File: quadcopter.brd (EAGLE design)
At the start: 151.1 x 125.5 mm, 66 parts, among them J1 AVR_SPI_PRG_6NS, Q1 2.6A, Q2 2.6A, Q3 2.6A, Q4 2.6A, U1 ATMEGA128RFA1, U2 IMU_LSM9DS1TR, Y1 16MHz

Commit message: tried some stuff on board
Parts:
- moved U2 117.0 mm to (0.00, 0.00), turned to 0 degrees
- moved C23 99.9 mm to (-3.00, 12.0)
- moved C20 98.9 mm to (-9.00, 2.00)
- moved C22 95.6 mm to (-7.00, 12.0)
- moved R8 89.8 mm to (-5.00, -3.00)
- moved C21 89.6 mm to (1.00, 7.00), turned to 0 degrees
- moved C25 86.0 mm to (3.00, 11.0), turned to 180 degrees
- moved U$3 21.2 mm to (91.8, -5.76)
- moved U1 9.85 mm to (165.0, -20.6)

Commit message: added board stuff
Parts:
- moved U1 190.8 mm to (-24.7, -0.20), turned to 270 degrees
- moved U$2 176.4 mm to (-55.9, 2.10), turned to 180 degrees
- moved C2 171.1 mm to (-65.6, 1.80), turned to 180 degrees
- moved D1 151.0 mm to (-56.6, -2.40), turned to 180 degrees
- moved Q1 148.6 mm to (-49.9, -2.20)
- moved Y1 148.3 mm to (-28.4, 10.4), turned to 180 degrees
- moved JP2 147.2 mm to (-29.8, -29.9)
- moved U$1 140.6 mm to (-31.5, 30.2)
- moved C3 138.8 mm to (-45.3, 2.20), turned to 180 degrees
- moved D9 137.4 mm to (-10.0, 28.0), turned to 180 degrees
- moved D5 137.2 mm to (0.03, -27.6), flipped to the bottom, turned to 0 degrees
- moved C16 135.1 mm to (-33.5, 15.2)
- moved U$4 134.8 mm to (2.40, -58.0)
- moved C19 134.0 mm to (-21.5, 29.2), turned to 180 degrees
- moved D6 133.4 mm to (0.00, -27.6), turned to 180 degrees
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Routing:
- added copper zone on layer 2, net 3V
- added copper zone on layer 1, net GND
- added copper zone on layer 15, net GND
- added copper zone on layer 2, net GND
- added copper zone on layer 2, net VBAT
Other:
- board size 151.1 x 125.5 mm -> 185.1 x 185.1 mm

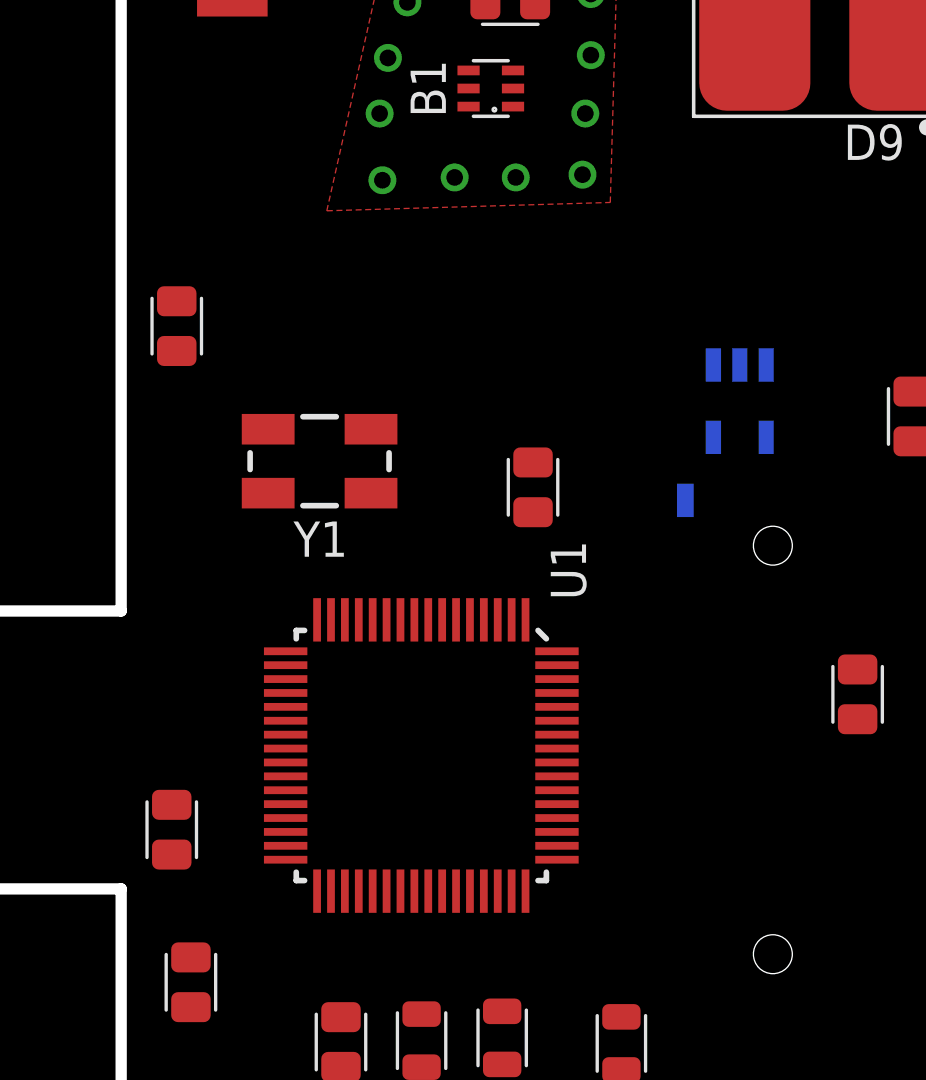
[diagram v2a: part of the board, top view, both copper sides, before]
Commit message: Restricting the Autorouter- setting trace widths - done?
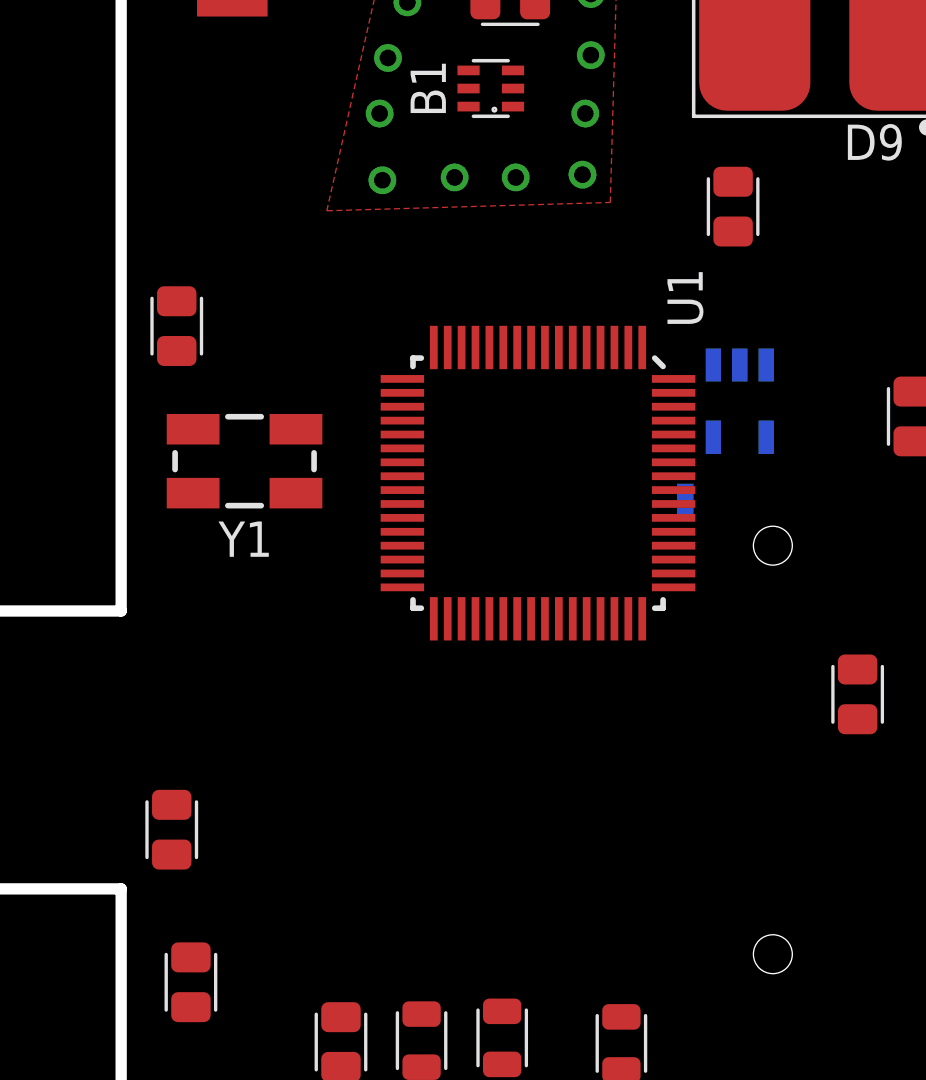
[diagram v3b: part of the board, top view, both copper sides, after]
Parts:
- moved C14 12.4 mm to (-13.5, 19.6)
- moved U1 10.7 mm to (-20.5, 9.60)
- moved Y1 2.70 mm to (-31.1, 10.4)
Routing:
- added copper zone on layer 2, net N$35
- added copper zone on layer 15, net N$36

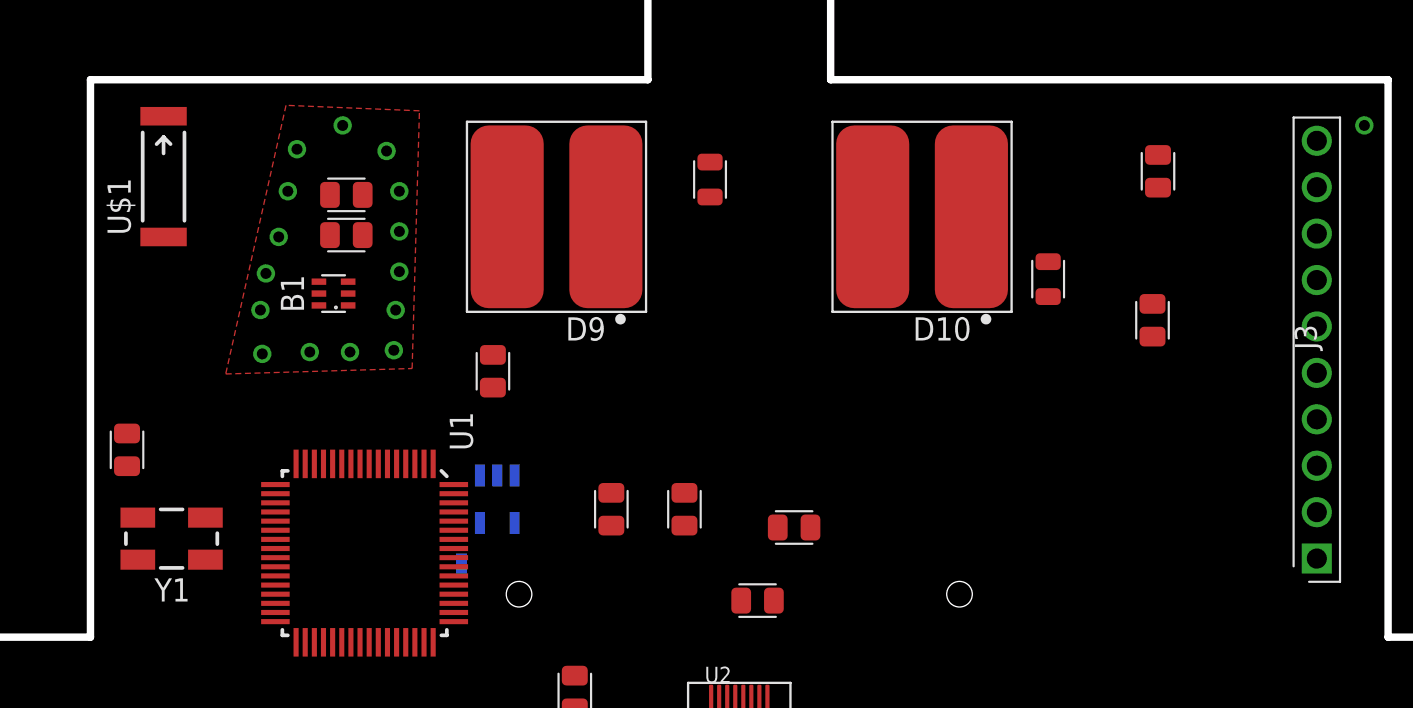
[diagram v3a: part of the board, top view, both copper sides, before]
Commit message: did the imu protection, voltage regulator, breakout header stuff:
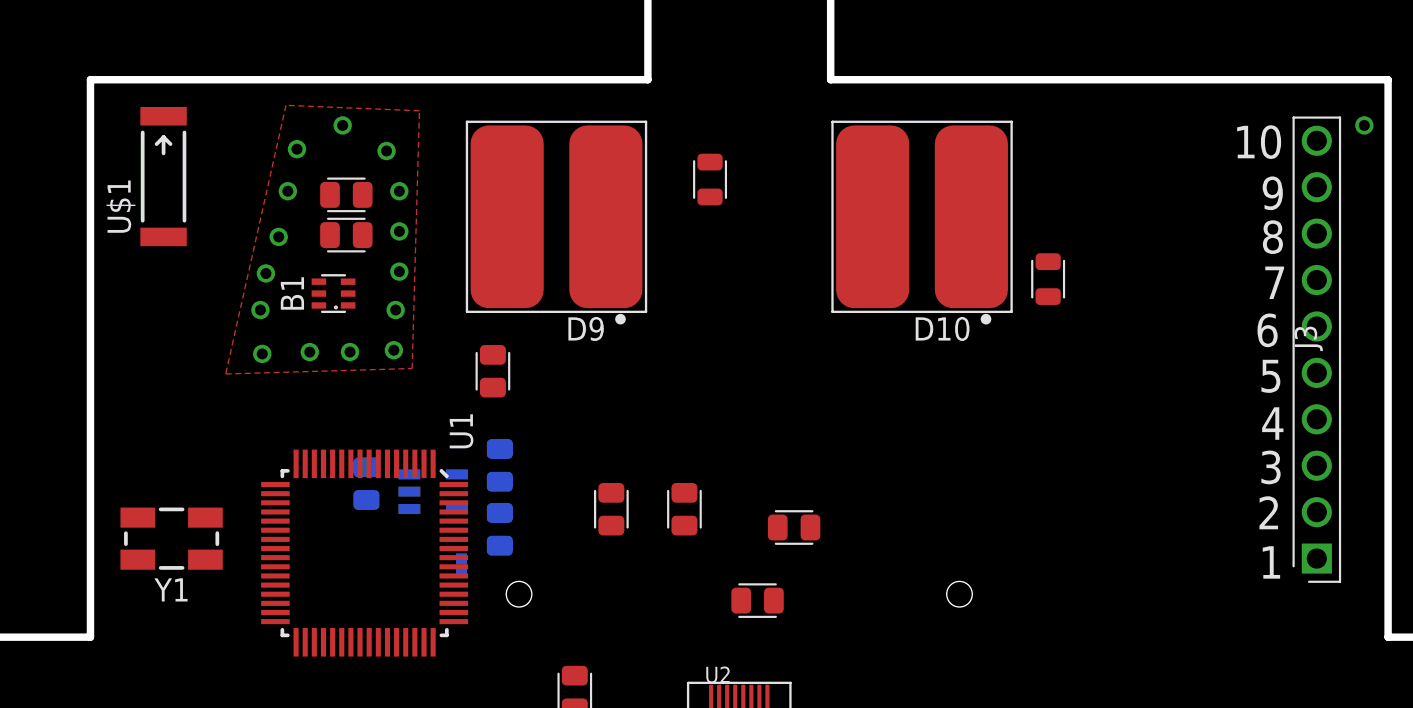
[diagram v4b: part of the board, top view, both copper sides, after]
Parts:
- moved C10 43.9 mm to (-20.4, 13.4), flipped to the bottom, turned to 270 degrees
- moved C11 39.4 mm to (-13.1, 14.4), flipped to the bottom, turned to 270 degrees
- moved C16 20.9 mm to (-13.1, 10.9), flipped to the bottom, turned to 270 degrees
- moved U$3 3.53 mm to (-16.8, 13.0), turned to 90 degrees
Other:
- board text added: "1"
- board text added: "10"
- board text added: "2"
- board text added: "3"
- board text added: "4"
- board text added: "5"
- board text added: "6"
- board text added: "7"
- board text added: "8"
- board text added: "9"

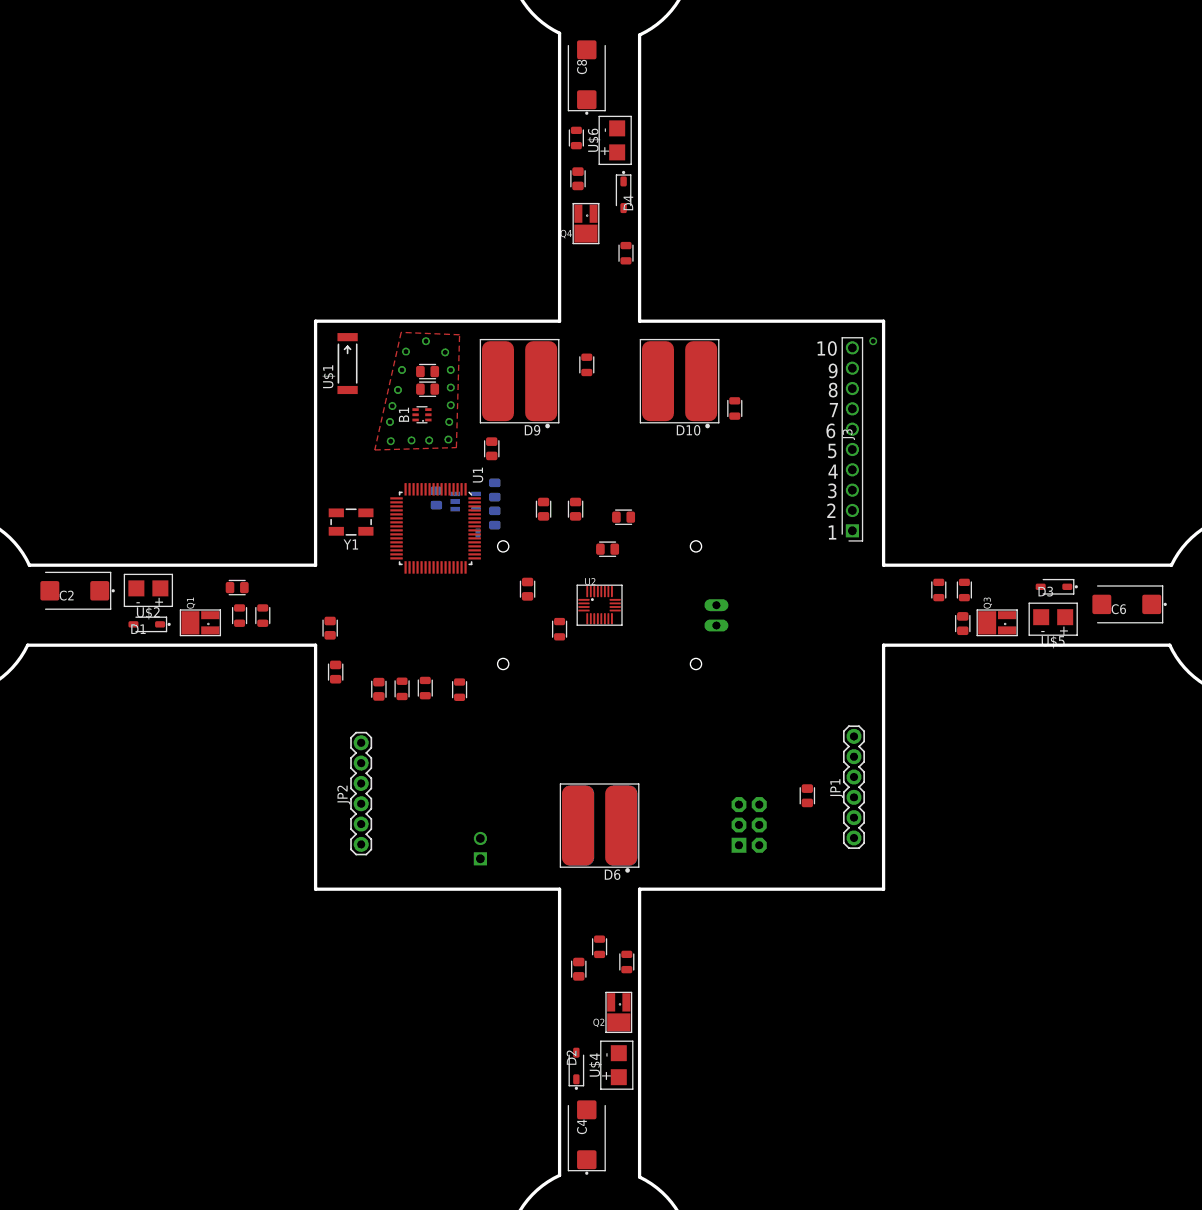
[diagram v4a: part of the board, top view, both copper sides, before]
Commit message: polygons may have fallen apart
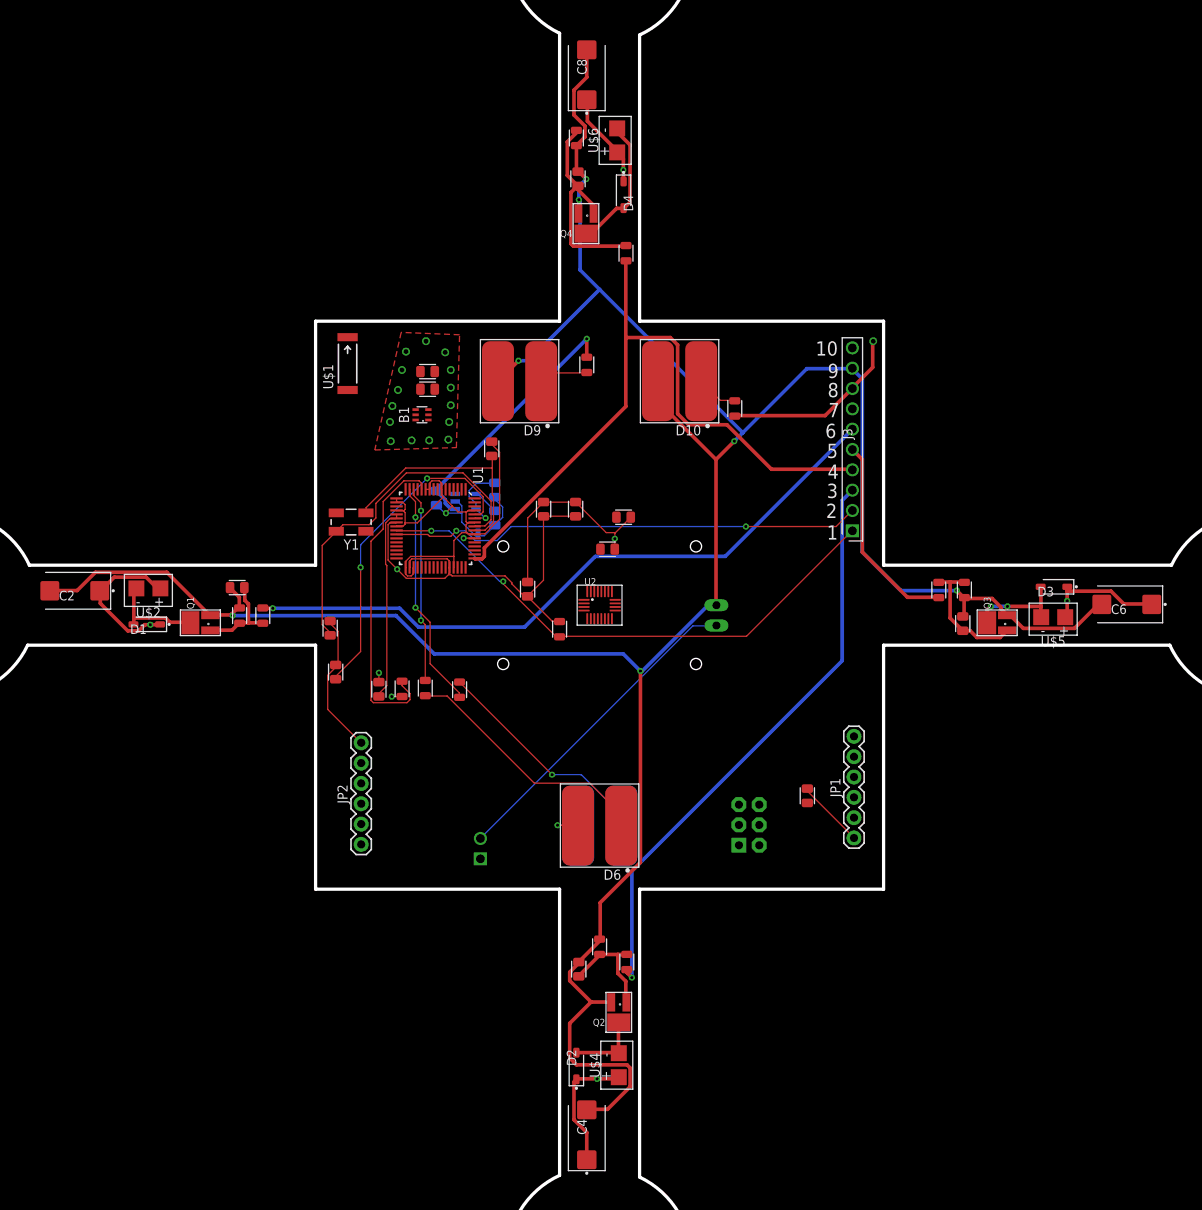
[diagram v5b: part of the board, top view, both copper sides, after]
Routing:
- net BAT_GND: track 0.00 -> 363.1 mm, vias 0 -> 7
- net GND: track 0.00 -> 158.6 mm, vias 15 -> 19
- net VBAT: track 0.00 -> 120.4 mm, vias 1 -> 6
- net PE3: track 0.00 -> 85.9 mm
- net PB5: track 0.00 -> 84.9 mm, vias 0 -> 1
- net PE4: track 0.00 -> 73.6 mm, vias 0 -> 1
- net SCL: track 0.00 -> 68.2 mm, vias 0 -> 2
- net 3V: track 0.00 -> 65.4 mm, vias 0 -> 4
- net SDA: track 0.00 -> 59.4 mm, vias 0 -> 2
- net N$5: track 0.00 -> 43.8 mm
- net N$10: track 0.00 -> 40.9 mm, vias 0 -> 2
- net N$23: track 0.00 -> 40.5 mm
- net RESET: track 0.00 -> 40.1 mm
- net N$28: track 0.00 -> 32.0 mm
- net N$14: track 0.00 -> 29.6 mm
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
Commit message: no more airwires!
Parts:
- moved NET_BRIDGE 5.78 mm to (-20.8, 10.5), turned to 0 degrees
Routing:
- net PE5: track 25.3 -> 91.6 mm, vias 0 -> 3
- net PE4: track 73.6 -> 120.2 mm, vias 1 -> 4
- net 3V: track 65.4 -> 89.9 mm, vias 4 -> 6
- net GND: track 158.6 -> 180.2 mm
- net SDA: track 59.4 -> 80.9 mm, vias 2 -> 5
- net BAT_GND: track 363.1 -> 382.9 mm, vias 7 -> 9
- net RFANT: track 0.00 -> 16.3 mm
- net N$15: track 0.00 -> 12.5 mm
- net N$22: track 0.00 -> 11.6 mm
- net N$21: track 0.00 -> 9.82 mm
- net SCL: track 68.2 -> 76.4 mm, vias 2 -> 4
- net PB5: track 84.9 -> 92.4 mm, vias 1 -> 2
- net N$17: track 0.00 -> 5.42 mm

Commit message: Some changes to brd
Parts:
- moved C12 33.6 mm to (-7.80, 13.9), turned to 0 degrees
- moved C15 32.6 mm to (-4.20, 11.1)
- moved Y1 23.3 mm to (-7.81, 9.26), turned to 90 degrees
- moved C13 21.6 mm to (-30.8, 10.8), turned to 180 degrees
- moved C14 15.2 mm to (-4.20, 7.50), turned to 270 degrees
- moved J1 11.5 mm to (19.3, -16.0), flipped to the top
- moved U$1 11.1 mm to (-20.4, 29.7)
- moved C18 6.18 mm to (-23.9, 21.3)
- moved C19 6.09 mm to (-23.9, 23.6), turned to 0 degrees
- moved C22 5.61 mm to (-6.70, 17.6)
- moved C23 3.79 mm to (-2.20, 15.7)
- moved B1 3.02 mm to (-20.5, 21.3), turned to 270 degrees
- moved C11 0.10 mm to (-13.1, 14.5)
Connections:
- net GND: now also B1.5; no longer B1.3
- net N$21: now also B1.4; no longer B1.1
- net N$22: now also B1.3; no longer B1.5
- net N$25: now also B1.2
- net RFANT: now also B1.1; no longer B1.4
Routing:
- net BAT_GND: track 382.9 -> 0.00 mm, vias 9 -> 0
- net GND: track 180.2 -> 0.00 mm, vias 19 -> 0
- net VBAT: track 120.4 -> 0.00 mm, vias 6 -> 0
- net PE4: track 120.2 -> 0.00 mm, vias 4 -> 0
- net PB5: track 92.4 -> 0.00 mm, vias 2 -> 0
- net PE5: track 91.6 -> 0.00 mm, vias 3 -> 0
- net 3V: track 89.9 -> 0.00 mm, vias 6 -> 0
- net PE3: track 85.9 -> 0.00 mm
- net SDA: track 80.9 -> 0.00 mm, vias 5 -> 0
- net SCL: track 76.4 -> 0.00 mm, vias 4 -> 0
- net N$5: track 43.8 -> 0.00 mm
- net N$10: track 40.9 -> 0.00 mm, vias 2 -> 0
- net N$23: track 40.5 -> 0.00 mm
- net RESET: track 40.1 -> 0.00 mm
- net N$28: track 32.0 -> 0.00 mm
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
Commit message: Wired up
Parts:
- C14, C15: value 12pF -> 1uF
- C2, C4, C6, C8: value 100uF -> 220uF
- D1, D2, D3, D4: value 20V-500MA -> (none)
- moved C10 45.3 mm to (20.7, -5.60)
- moved C11 43.0 mm to (25.9, -3.60)
- moved C16 41.2 mm to (26.5, -0.30), turned to 180 degrees
- moved NET_BRIDGE 41.1 mm to (19.3, 1.30)
- moved U$3 40.5 mm to (21.1, -1.40)
- moved J2 38.3 mm to (15.5, -8.40), flipped to the top
- moved D5 18.7 mm to (-17.8, -21.9)
- moved R6 18.4 mm to (0.10, 40.2), turned to 180 degrees
- moved D6 17.8 mm to (-17.8, -28.2)
- moved C2 17.3 mm to (-48.3, 2.00), turned to 0 degrees
- moved C6 15.8 mm to (50.2, -1.90)
- moved C23 15.5 mm to (8.20, 4.20), turned to 0 degrees
- moved C3 15.3 mm to (-30.3, -0.80), turned to 90 degrees
- moved C4 14.7 mm to (-1.80, -51.5)
- moved R2 14.5 mm to (27.9, 2.50), turned to 0 degrees
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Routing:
- net VBAT: track 0.00 -> 319.5 mm, vias 0 -> 3
- net BAT_GND: track 0.00 -> 255.6 mm, vias 0 -> 4
- net GND: track 0.00 -> 195.8 mm, vias 0 -> 4
- net PE4: track 0.00 -> 95.0 mm
- net PB5: track 0.00 -> 94.5 mm, vias 0 -> 2
- net PE3: track 0.00 -> 76.9 mm, vias 0 -> 2
- net SDA: track 0.00 -> 73.4 mm, vias 0 -> 4
- net SCL: track 0.00 -> 72.2 mm, vias 0 -> 3
- net 3V: track 0.00 -> 69.1 mm, vias 0 -> 9
- net PE5: track 0.00 -> 64.6 mm
- net N$26: track 0.00 -> 41.5 mm, vias 0 -> 2
- net RESET: track 0.00 -> 40.7 mm
- net N$20: track 0.00 -> 40.0 mm
- net N$24: track 0.00 -> 33.7 mm
- net N$16: track 0.00 -> 23.0 mm
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- removed copper zone on layer 1, net GND
- removed copper zone on layer 2, net N$35
- removed copper zone on layer 15, net N$36
